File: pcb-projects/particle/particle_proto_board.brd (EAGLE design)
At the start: 36.8 x 35.6 mm, 53 parts, among them IC1 ATTINY20-MMH, IC2 DMC2400V, IC3 DMC2400V, SW1 SW1, SW2 SW2, SW3 SW3

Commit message: fixed typo in schema
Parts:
- GND_B: value GND_b -> GND_B
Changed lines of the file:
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@@
 <element name="VCC_B" library="wirepad" package="1,6/0,9" value="VCC_B" x="1.905" y="31.115"/>
 <element name="GND_A" library="wirepad" package="1,6/0,9" value="GND_A" x="33.655" y="2.54"/>
-<element name="GND_B" library="wirepad" package="1,6/0,9" value="GND_b" x="33.655" y="31.115"/>
+<element name="GND_B" library="wirepad" package="1,6/0,9" value="GND_B" x="33.655" y="31.115"/>
 <element name="RXB" library="wirepad" package="1,6/0,9" value="RXB" x="27.305" y="30.48" rot="R90"/>
 <element name="TXB" library="wirepad" package="1,6/0,9" value="TXB" x="20.32" y="30.48" rot="R90"/>

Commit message: solved #34, solved #33, solved #32
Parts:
- RESET, SWLED1, SWLED3, SWLED4, SWLED5, SWLED6: device jumper:SJ -> jumper-switches:SJ
- SW1, SW2, SW3: device jumper:SJ_2 -> jumper-switches:SJ_2
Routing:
- net RX_B: track 20.6 -> 21.3 mm

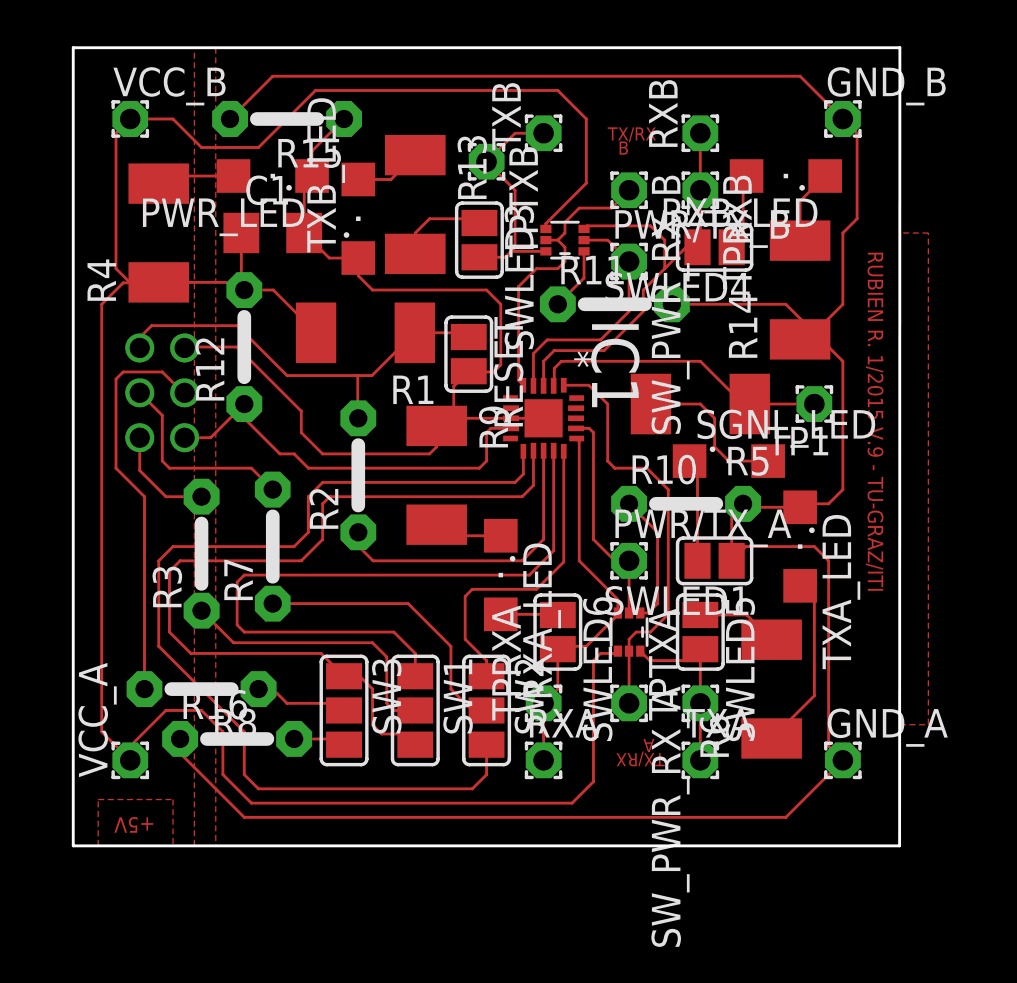
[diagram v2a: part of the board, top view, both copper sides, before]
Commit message: added several sparkfun and one samtec library, fixed #39, fixed #37, fixed #36, fixed #35, fixed #29
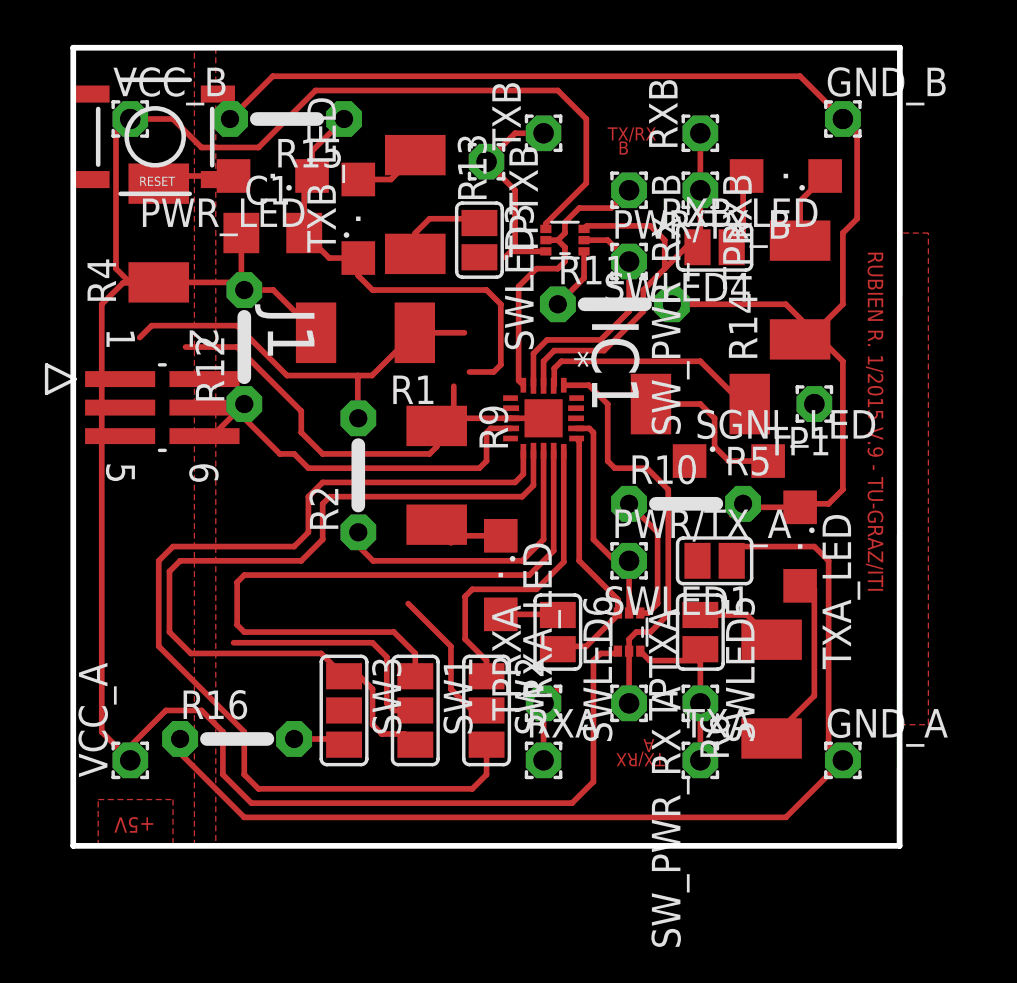
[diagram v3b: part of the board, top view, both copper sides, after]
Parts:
- removed PI: 332-06, con-garry:332-06
- removed R3, R7, R8: (no value), jumper:05
- added J1: FTS-103-01-L-DV, samtec-FTS-103-01-L-DV:SAMTEC_FTS-103-01-L-DV
- RESET: value RESET -> SWITCH-MOMENTARY-2SMD; device jumper-switches:SJ -> SparkFun-Electromechanical:TACTILE-SWITCH-SMD
- moved RESET 17.0 mm to (3.02, 30.3), turned to 180 degrees
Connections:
- removed net N$16: R8.1, SW3.2
- removed net N$19: PI.4, R8.2
- removed net N$21: PI.1, R3.2
- net GND: now also J1.6, RESET.1, SGNL_LED.C; no longer PI.6, RESET.2, SWLED1.1
- net N$1: now also J1.1; no longer R3.1
- net N$11: now also SWLED1.2; no longer R5.1
- net N$15: now also J1.4, SW3.2; no longer PI.3, R7.2
- net N$20: now also J1.3; no longer R7.1
- net N$23: now also R5.1, SWLED1.1; no longer SGNL_LED.C, SWLED1.2
- net RESET: now also J1.5, RESET.3; no longer PI.5, RESET.1
- net VCC: now also J1.2; no longer PI.2
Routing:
- net N$19: track 17.9 -> 0.00 mm
- net N$15: track 8.90 -> 0.00 mm
- net N$20: track 12.6 -> 6.58 mm
- net N$21: track 4.70 -> 0.00 mm
- net N$23: track 4.59 -> 0.00 mm
- net N$16: track 4.20 -> 0.00 mm
- net GND: track 154.8 -> 150.8 mm
- net N$11: track 13.3 -> 10.1 mm
- net N$1: track 12.6 -> 10.6 mm
- net RX_A: track 17.2 -> 15.3 mm
- net VCC: track 121.2 -> 120.0 mm
- net TX_B: track 10.7 -> 9.59 mm
- net RESET: track 19.0 -> 18.3 mm
- net TX_A: track 7.80 -> 7.29 mm

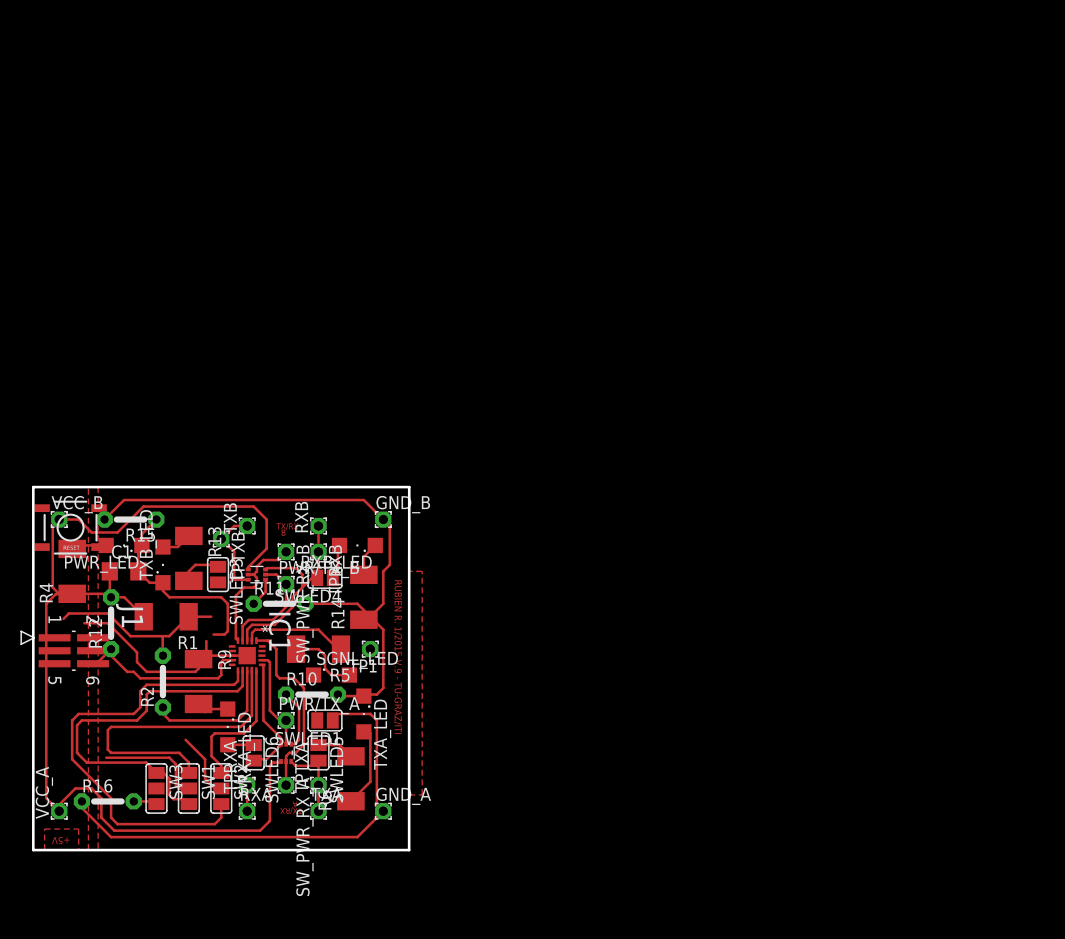
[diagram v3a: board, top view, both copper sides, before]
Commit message: fixed #41, fixed #40, fixed #39, fixed #37, fixed #35, fixed #29
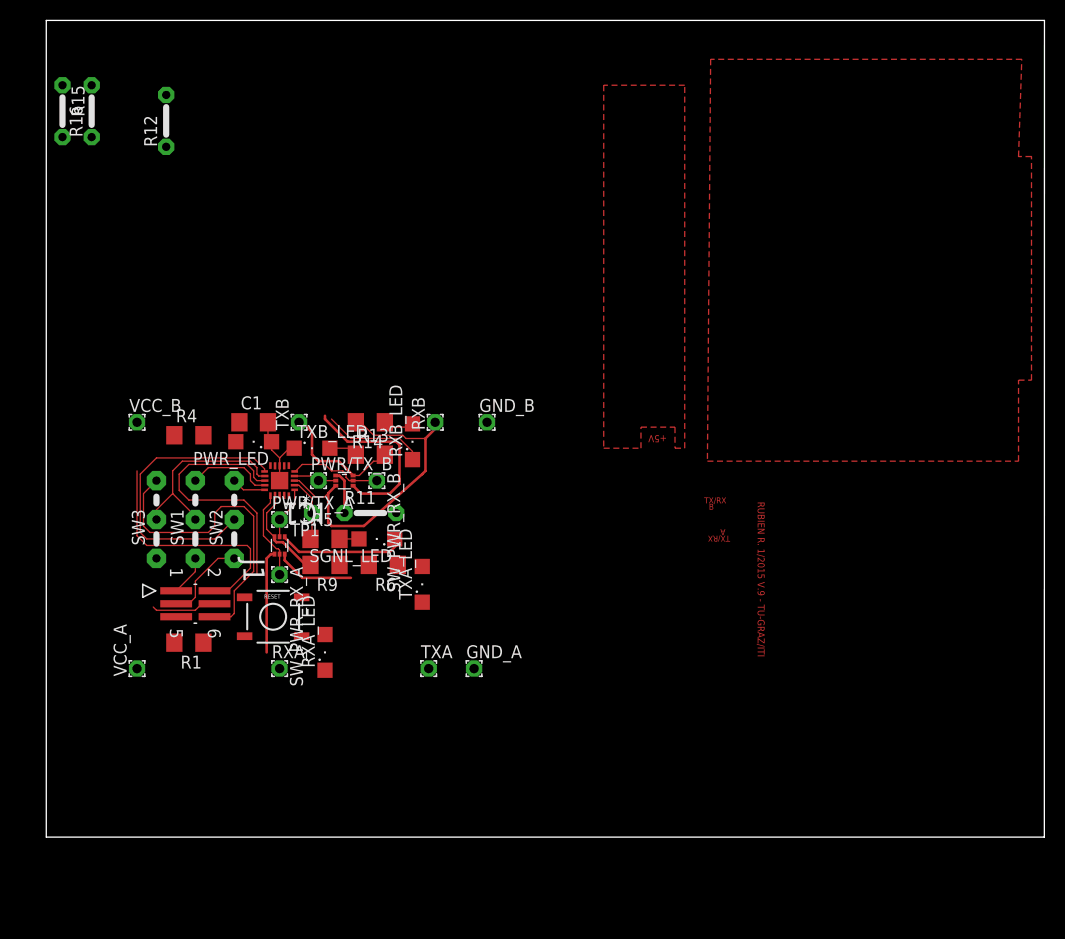
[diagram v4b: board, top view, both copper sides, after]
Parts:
- removed R10, R2: (no value), jumper:05
- removed SWLED1: J5, jumper-switches:SJ
- removed SWLED3: J2, jumper-switches:SJ
- removed SWLED4: J4, jumper-switches:SJ
- removed SWLED5: J1, jumper-switches:SJ
- removed SWLED6: J3, jumper-switches:SJ
- removed TPRXA: TPRXA, wirepad:1,6/0,9
- removed TPRXB: TPRXB, wirepad:1,6/0,9
- removed TPTXA: TPTXA, wirepad:1,6/0,9
- removed TPTXB: TPTXB, wirepad:1,6/0,9
- R1, R13, R14, R4, R5, R6, R9: device rcl:R2010 -> rcl:R1206
- SW1: value SW1 -> T/S-PI SW; device jumper-switches:SJ_2 -> jumper-switches:04C
- SW2: value SW2 -> T/S-PI SW; device jumper-switches:SJ_2 -> jumper-switches:04C
- SW3: value SW3 -> T/S-PI SW; device jumper-switches:SJ_2 -> jumper-switches:04C
- moved R16 67.6 mm to (5.08, 71.1), turned to 90 degrees
- moved R12 49.5 mm to (12.4, 70.2)
- moved R15 40.6 mm to (2.22, 71.1), turned to 270 degrees
- moved SW2 24.5 mm to (19.1, 29.2), turned to 90 degrees
- moved SW1 24.5 mm to (15.2, 29.2), turned to 90 degrees
- moved SW3 24.4 mm to (11.4, 29.2), turned to 90 degrees
- moved RESET 21.7 mm to (22.9, 21.6), turned to 0 degrees
- moved R6 21.2 mm to (33.7, 26.7), turned to 180 degrees
- moved SW_PWR_RX_A 20.6 mm to (23.5, 25.7)
- moved R13 20.5 mm to (32.4, 37.5), turned to 0 degrees
- moved IC2 20.3 mm to (23.5, 28.6)
- moved PWR/TX_A 19.7 mm to (23.5, 31.1)
- moved C1 19.4 mm to (21.0, 40.6)
- moved TXB_LED 18.5 mm to (26.7, 38.1), turned to 0 degrees
- moved TXA 17.7 mm to (38.1, 16.5)
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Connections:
- removed net N$11: IC1.2, SWLED1.2, TP1.1
- removed net N$12: RXA_LED.A, SWLED6.1
- removed net N$14: R6.2, SWLED5.1
- removed net N$2: IC1.13, R2.1
- removed net N$24: IC2.1, R10.1
- removed net N$6: R13.2, SWLED3.1
- removed net N$7: RXB_LED.A, SWLED4.1
- net GND: now also IC2.1, RXA_LED.C, RXB_LED.C; no longer R10.2, R14.1, R9.1
- net N$1: now also SW1.1; no longer SW1.2
- net N$15: now also SW3.1; no longer SW3.2
- net N$20: now also SW2.1; no longer SW2.2
- net N$23: now also IC1.2, TP1.1; no longer SWLED1.1
- net N$4: now also R9.1, RXA_LED.A; no longer R9.2, RXA_LED.C
- net N$8: now also R14.1, RXB_LED.A; no longer R14.2, RXB_LED.C
- net PWR/TX_A: now also IC1.1; no longer IC1.17
- net RESET: now also IC1.13; no longer R2.2
- net RX_A: now also IC1.17, R9.2; no longer IC1.16, SWLED6.2, TPRXA.1
- net RX_B: now also R14.2; no longer SWLED4.2, TPRXB.1
- net SPI_MISO: now also SW1.3; no longer SW1.1
- net SPI_SCK: now also SW2.3; no longer SW2.1
- net SW_PWR/RX_A: now also IC1.16; no longer IC1.1
- net TPI_CLK: now also SW2.2; no longer SW2.3
- net TPI_DATA/SPI_MOSI: now also SW1.2, SW3.2; no longer SW1.3, SW3.1
- net TX_A: now also R6.2; no longer SWLED5.2, TPTXA.1
- net TX_B: now also R13.2; no longer SWLED3.2, TPTXB.1
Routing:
- net GND: track 150.8 -> 61.2 mm
- net VCC: track 120.0 -> 52.2 mm
- net SPI_MISO: track 30.5 -> 8.42 mm
- net TPI_DATA/SPI_MOSI: track 37.0 -> 19.3 mm
- net TPI_CLK: track 43.5 -> 29.5 mm
- net N$2: track 13.5 -> 0.00 mm
- net RX_B: track 21.1 -> 33.4 mm
- net SPI_SCK: track 13.9 -> 3.34 mm
- net N$11: track 10.1 -> 0.00 mm
- net SW_PWR/RX_A: track 18.7 -> 8.77 mm
- net N$3: track 8.13 -> 0.00 mm
- net RESET: track 18.3 -> 26.0 mm
- net PWR/TX_B: track 11.1 -> 4.24 mm
- net N$1: track 10.6 -> 3.95 mm
- net N$15: track 0.00 -> 6.40 mm
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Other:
- board size 36.8 x 35.6 mm -> 97.8 x 80 mm

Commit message: routed board after several changes to schema
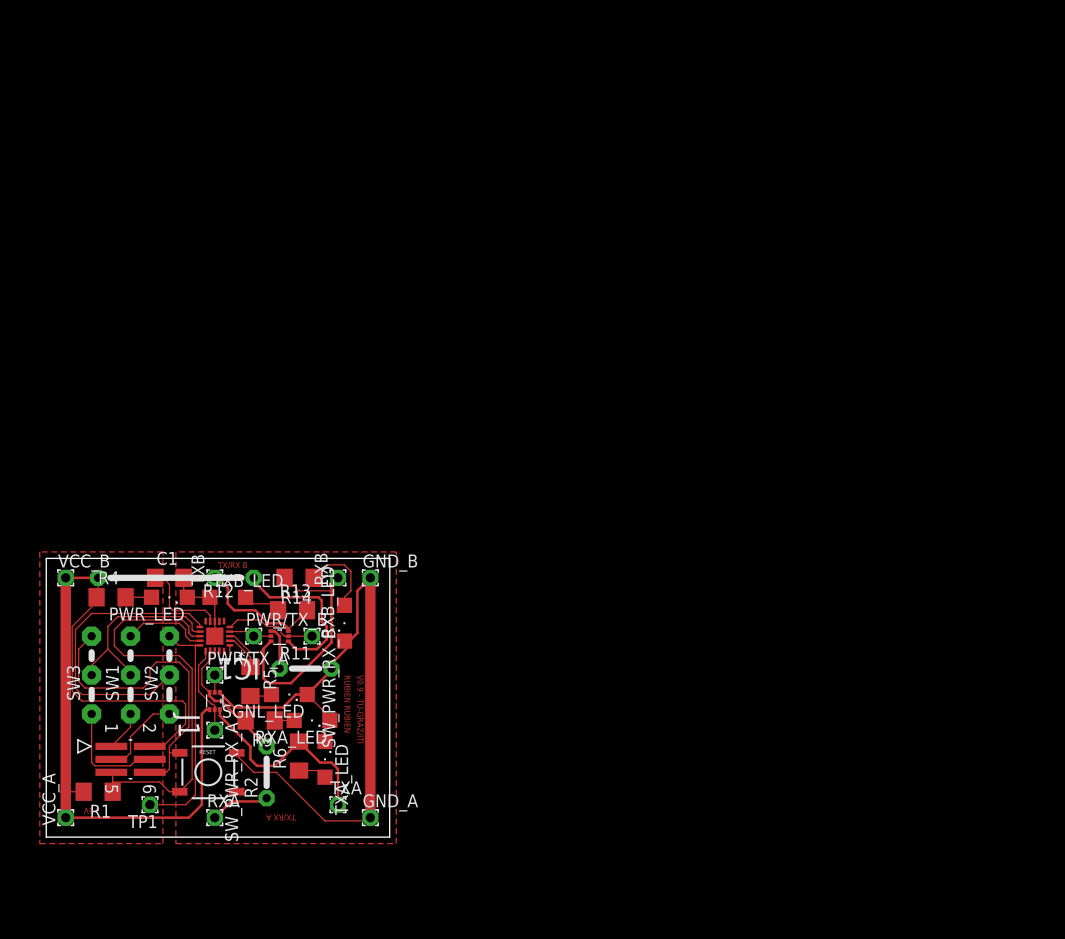
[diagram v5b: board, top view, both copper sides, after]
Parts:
- removed R15, R16: J5MM, jumper:05
- added R2: J5MM, jumper:05
- R12: value J5MM -> J15MM; device jumper:05 -> jumper:15
- moved R12 44.8 mm to (13.3, 25.4), turned to 180 degrees
- moved TP1 32.7 mm to (10.8, 3.17)
- moved R6 20.5 mm to (25.4, 7.94), turned to 90 degrees
- moved TXA_LED 19.6 mm to (27.9, 7.62), turned to 270 degrees
- moved GND_B 19.1 mm to (32.4, 25.4)
- moved RXB_LED 19.0 mm to (29.8, 21.0)
- moved RXB 18.0 mm to (29.2, 25.4)
- moved GND_A 17.8 mm to (32.4, 1.91)
- moved R4 17.6 mm to (6.99, 23.5)
- moved SGNL_LED 17.5 mm to (24.4, 14.0)
- moved C1 17.3 mm to (12.7, 25.4)
- moved TXB 17.3 mm to (17.1, 25.4)
- moved PWR_LED 17.3 mm to (12.7, 23.5)
- moved R1 17.1 mm to (5.71, 4.45)
- moved R13 17.0 mm to (24.8, 22.2)
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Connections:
- new net N$2: R2.1, RXA.1
- net GND: no longer R15.1, R15.2, R16.1, R16.2
- net N$23: no longer TP1.1
- net RX_A: now also R2.2; no longer RXA.1
- net SPI_SCK: now also TP1.1
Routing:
- net VCC: track 52.2 -> 107.3 mm
- net GND: track 61.2 -> 109.7 mm
- net SPI_SCK: track 3.34 -> 23.3 mm
- net RESET: track 26.0 -> 41.4 mm
- net TX_A: track 8.28 -> 20.5 mm
- net N$8: track 3.03 -> 8.98 mm
- net N$2: track 0.00 -> 5.87 mm
- net N$15: track 6.40 -> 10.8 mm
- net RX_B: track 33.4 -> 29.5 mm
- net RX_A: track 9.41 -> 13.0 mm
- net N$3: track 0.00 -> 2.81 mm
- net N$23: track 6.30 -> 3.67 mm
- net N$22: track 0.00 -> 2.54 mm
- net N$4: track 0.00 -> 1.91 mm
- net N$13: track 3.44 -> 4.34 mm
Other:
- board size 97.8 x 80 mm -> 33.7 x 27.3 mm
- board text added: "RUBIEN RUBIEN"
- board text added: "V0.9 - TU-GRAZ/ITI"
- board text removed: "RUBIEN R. 1/2015 V.9 - TU-GRAZ/ITI"

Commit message: closed #44, closed #43, closed #42
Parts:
- removed R11: (no value), jumper:05
- removed R12: J15MM, jumper:15
- removed R2: J5MM, jumper:05
- moved PWR_LED 2.54 mm to (10.2, 23.5)
- moved R4 1.90 mm to (6.99, 25.4)
- moved TXB_LED 1.90 mm to (16.5, 23.5)
- moved TXA 1.27 mm to (29.2, 1.91)
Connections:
- removed net N$17: IC3.1, R11.1
- removed net N$2: R2.1, RXA.1
- net GND: now also IC3.1; no longer R11.2
- net RX_A: now also RXA.1; no longer R2.2
- net VCC: no longer R12.1, R12.2
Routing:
- net GND: track 109.7 -> 141.1 mm, vias 0 -> 2
- net VCC: track 107.3 -> 127.0 mm, vias 0 -> 2
- net RX_A: track 13.0 -> 24.0 mm, vias 0 -> 2
- net N$2: track 5.87 -> 0.00 mm
- net N$17: track 4.23 -> 0.00 mm
- net N$13: track 4.34 -> 6.25 mm
- net TX_A: track 20.5 -> 21.8 mm
- net TX_B: track 13.2 -> 14.2 mm
- net N$22: track 2.54 -> 1.91 mm
- net RX_B: track 29.5 -> 28.9 mm
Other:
- board size 33.7 x 27.3 mm -> 33.7 x 27.9 mm
